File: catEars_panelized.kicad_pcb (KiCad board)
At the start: 2 copper layers, 98.5 x 98.8 mm, 276 parts, among them J1 Conn_01x03_Socket, J2 Conn_01x03_Socket, U1 ESP-01v090, U1_ PinSocket_2x04_P2.54mm_Vertic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, U2 AMS1117-3.3

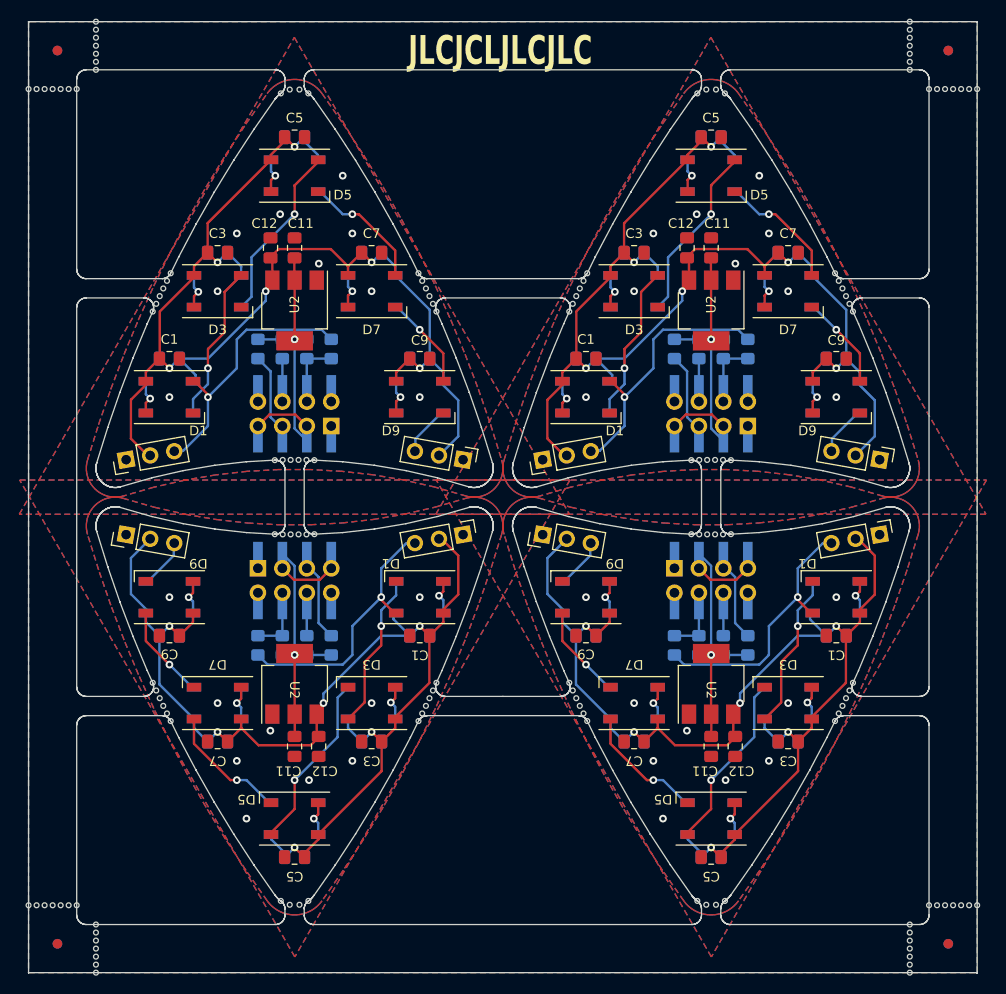
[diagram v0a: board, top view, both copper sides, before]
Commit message: changed C11 value
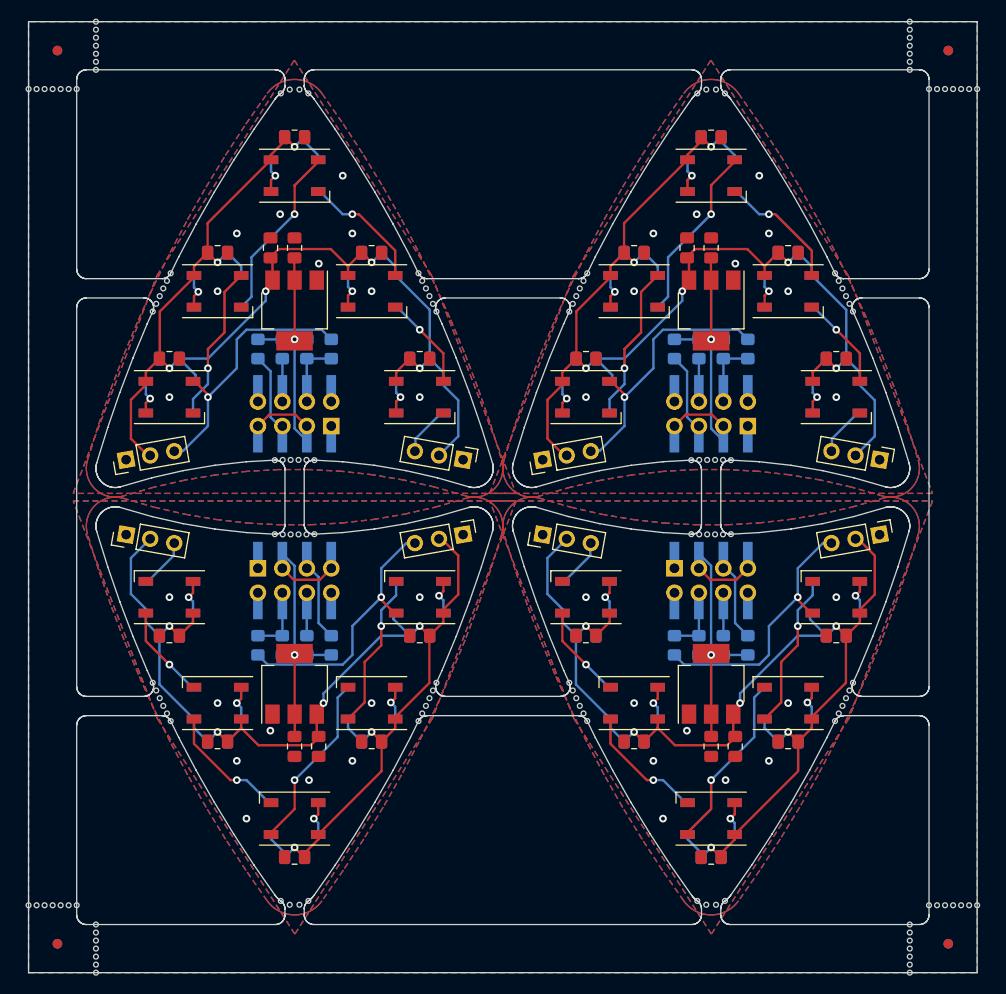
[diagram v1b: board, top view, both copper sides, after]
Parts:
- C11 (x4): value 220uF -> 22uF
- U1_ (x4): value PinSocket_2x04_P2.54mm_Vertical_SMD -> (none)
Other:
- outline, holes or cut-outs redrawn
- board text removed: "JLCJCLJLCJLC"
